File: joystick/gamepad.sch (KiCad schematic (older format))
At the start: 37 parts, among them IC1 ATTINY45-S, P2 CONN_01X04, SW1 SW_PUSH, SW2 SW_PUSH, SW3 SW_PUSH, SW4 SW_PUSH, SW5 SW_PUSH, SW6 SW_PUSH, U1 74LS165, U2 74164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

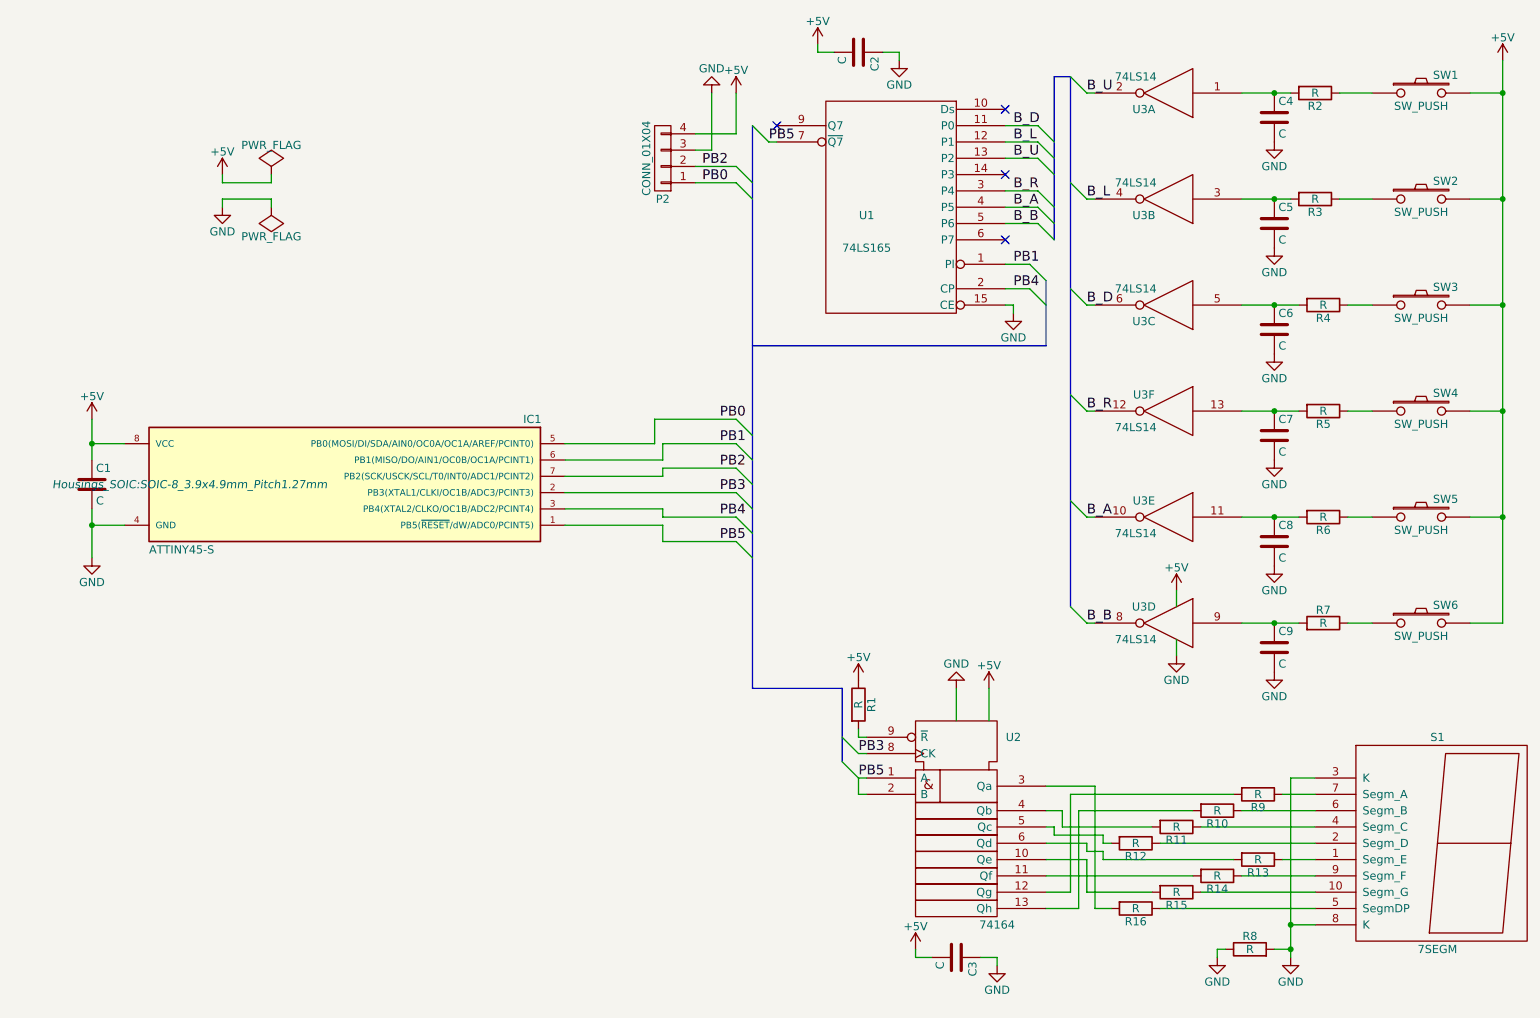
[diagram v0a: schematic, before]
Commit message: Updated joystick's circuit
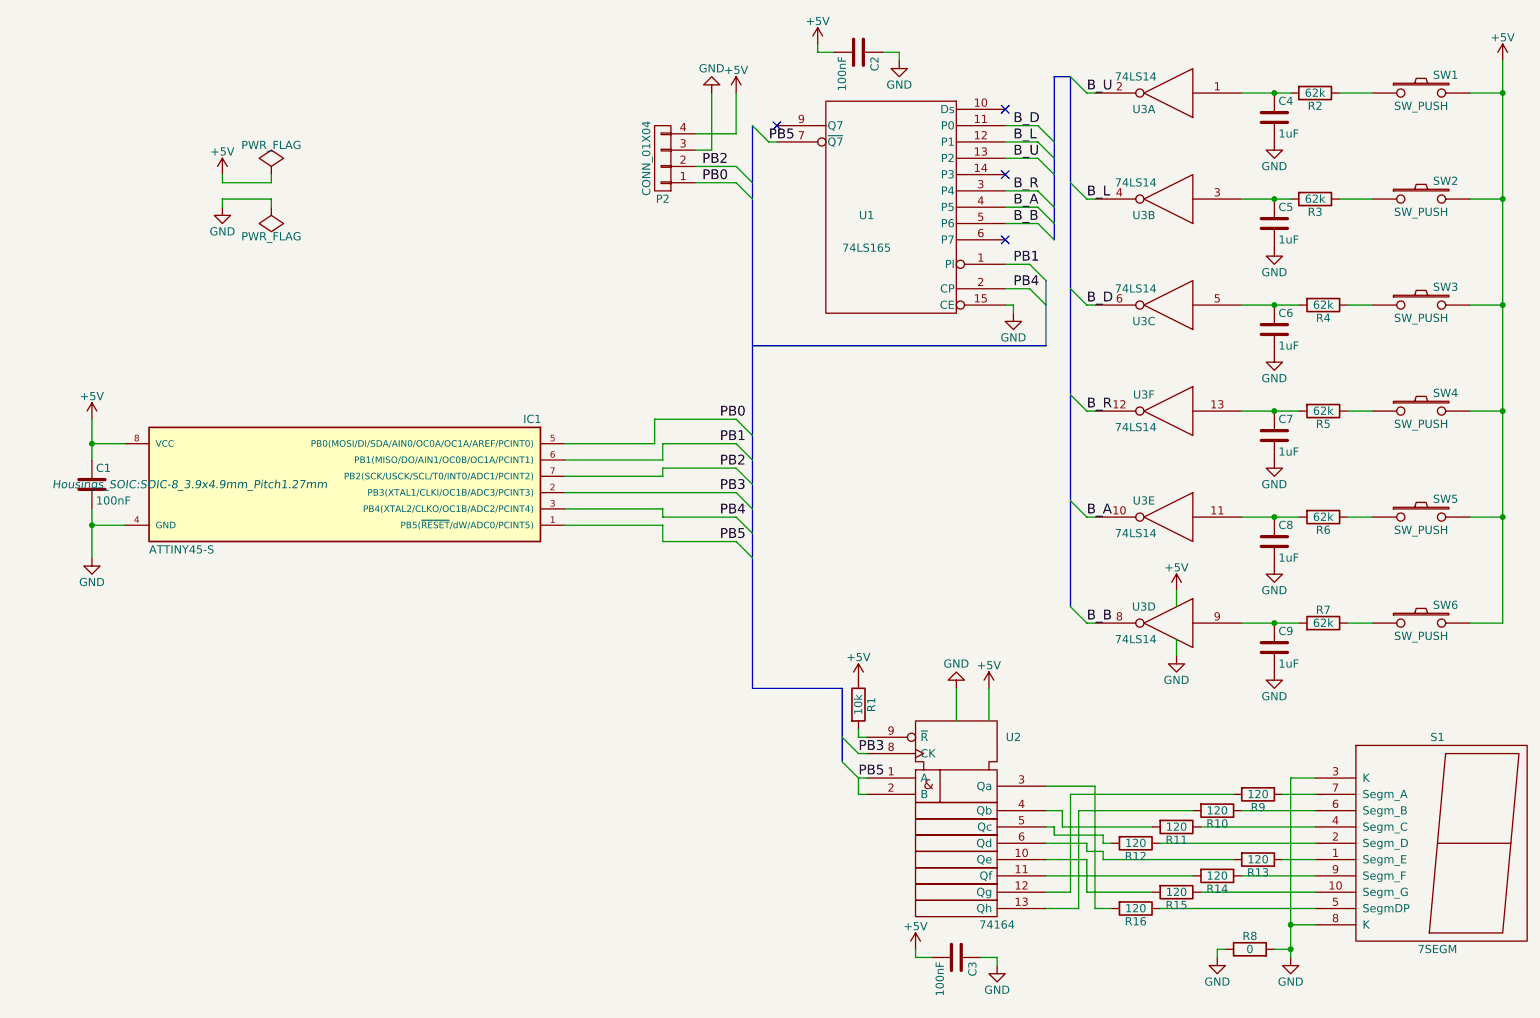
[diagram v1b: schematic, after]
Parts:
- C1, C2, C3: value C -> 100nF
- C4, C5, C6, C7, C8, C9: value C -> 1uF
- R1: value R -> 10k
- R10, R11, R12, R13, R14, R15, R16, R9: value R -> 120
- R2, R3, R4, R5, R6, R7: value R -> 62k
- R8: value R -> 0
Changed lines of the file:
@@
 P 8150 1000
 F 0 "R2" V 8230 1000 50  0000 C CNN
-F 1 "R" V 8150 1000 50  0000 C CNN
+F 1 "62k" V 8150 1000 50  0000 C CNN
 F 2 "Resistors_SMD:R_0805_HandSoldering" V 8080 1000 50  0001 C CNN
 F 3 "" H 8150 1000 50  0000 C CNN
@@
 P 7900 1150
 F 0 "C4" H 7925 1250 50  0000 L CNN
-F 1 "C" H 7925 1050 50  0000 L CNN
+F 1 "1uF" H 7925 1050 50  0000 L CNN
 F 2 "Capacitors_SMD:C_0805_HandSoldering" H 7938 1000 50  0001 C CNN
 F 3 "" H 7900 1150 50  0000 C CNN
@@
 P 8150 1650
 F 0 "R3" V 8230 1650 50  0000 C CNN
-F 1 "R" V 8150 1650 50  0000 C CNN
+F 1 "62k" V 8150 1650 50  0000 C CNN
 F 2 "Resistors_SMD:R_0805_HandSoldering" V 8080 1650 50  0001 C CNN
 F 3 "" H 8150 1650 50  0000 C CNN
@@
 P 7900 1800
 F 0 "C5" H 7925 1900 50  0000 L CNN
-F 1 "C" H 7925 1700 50  0000 L CNN
+F 1 "1uF" H 7925 1700 50  0000 L CNN
 F 2 "Capacitors_SMD:C_0805_HandSoldering" H 7938 1650 50  0001 C CNN
 F 3 "" H 7900 1800 50  0000 C CNN
@@
 P 7900 2450
 F 0 "C6" H 7925 2550 50  0000 L CNN
-F 1 "C" H 7925 2350 50  0000 L CNN
+F 1 "1uF" H 7925 2350 50  0000 L CNN
 F 2 "Capacitors_SMD:C_0805_HandSoldering" H 7938 2300 50  0001 C CNN
 F 3 "" H 7900 2450 50  0000 C CNN
@@
 P 8200 2300
 F 0 "R4" V 8280 2300 50  0000 C CNN
-F 1 "R" V 8200 2300 50  0000 C CNN
+F 1 "62k" V 8200 2300 50  0000 C CNN
 F 2 "Resistors_SMD:R_0805_HandSoldering" V 8130 2300 50  0001 C CNN
 F 3 "" H 8200 2300 50  0000 C CNN
@@
 P 7900 3100
 F 0 "C7" H 7925 3200 50  0000 L CNN
-F 1 "C" H 7925 3000 50  0000 L CNN
+F 1 "1uF" H 7925 3000 50  0000 L CNN
 F 2 "Capacitors_SMD:C_0805_HandSoldering" H 7938 2950 50  0001 C CNN
 F 3 "" H 7900 3100 50  0000 C CNN
@@
 P 8200 2950
 F 0 "R5" V 8280 2950 50  0000 C CNN
-F 1 "R" V 8200 2950 50  0000 C CNN
+F 1 "62k" V 8200 2950 50  0000 C CNN
 F 2 "Resistors_SMD:R_0805_HandSoldering" V 8130 2950 50  0001 C CNN
 F 3 "" H 8200 2950 50  0000 C CNN
@@
 P 7900 3750
 F 0 "C8" H 7925 3850 50  0000 L CNN
-F 1 "C" H 7925 3650 50  0000 L CNN
+F 1 "1uF" H 7925 3650 50  0000 L CNN
 F 2 "Capacitors_SMD:C_0805_HandSoldering" H 7938 3600 50  0001 C CNN
 F 3 "" H 7900 3750 50  0000 C CNN
@@
 P 8200 3600
 F 0 "R6" V 8280 3600 50  0000 C CNN
-F 1 "R" V 8200 3600 50  0000 C CNN
+F 1 "62k" V 8200 3600 50  0000 C CNN
 F 2 "Resistors_SMD:R_0805_HandSoldering" V 8130 3600 50  0001 C CNN
 F 3 "" H 8200 3600 50  0000 C CNN
@@
 P 7900 4400
 F 0 "C9" H 7925 4500 50  0000 L CNN
-F 1 "C" H 7925 4300 50  0000 L CNN
+F 1 "1uF" H 7925 4300 50  0000 L CNN
 F 2 "Capacitors_SMD:C_0805_HandSoldering" H 7938 4250 50  0001 C CNN
 F 3 "" H 7900 4400 50  0000 C CNN
@@
 P 8200 4250
 F 0 "R7" V 8280 4250 50  0000 C CNN
-F 1 "R" V 8200 4250 50  0000 C CNN
+F 1 "62k" V 8200 4250 50  0000 C CNN
 F 2 "Resistors_SMD:R_0805_HandSoldering" V 8130 4250 50  0001 C CNN
 F 3 "" H 8200 4250 50  0000 C CNN
@@
 P 650 3400
 F 0 "C1" H 675 3500 50  0000 L CNN
-F 1 "C" H 675 3300 50  0000 L CNN
+F 1 "100nF" H 675 3300 50  0000 L CNN
 F 2 "Capacitors_SMD:C_0805_HandSoldering" H 688 3250 50  0001 C CNN
 F 3 "" H 650 3400 50  0000 C CNN
@@
 P 5350 4750
 F 0 "R1" V 5430 4750 50  0000 C CNN
-F 1 "R" V 5350 4750 50  0000 C CNN
+F 1 "10k" V 5350 4750 50  0000 C CNN
 F 2 "Resistors_SMD:R_0805_HandSoldering" V 5280 4750 50  0001 C CNN
 F 3 "" H 5350 4750 50  0000 C CNN
@@
 P 5950 6300
 F 0 "C3" H 5975 6400 50  0000 L CNN
-F 1 "C" H 5975 6200 50  0000 L CNN
+F 1 "100nF" H 5975 6200 50  0000 L CNN
 F 2 "Capacitors_SMD:C_0805_HandSoldering" H 5988 6150 50  0001 C CNN
 F 3 "" H 5950 6300 50  0000 C CNN
@@
 P 5350 750
 F 0 "C2" H 5375 850 50  0000 L CNN
-F 1 "C" H 5375 650 50  0000 L CNN
+F 1 "100nF" H 5375 650 50  0000 L CNN
 F 2 "Capacitors_SMD:C_0805_HandSoldering" H 5388 600 50  0001 C CNN
 F 3 "" H 5350 750 50  0000 C CNN
@@
 P 7750 6250
 F 0 "R8" V 7830 6250 50  0000 C CNN
-F 1 "R" V 7750 6250 50  0000 C CNN
+F 1 "0" V 7750 6250 50  0000 C CNN
 F 2 "Resistors_SMD:R_0805_HandSoldering" V 7680 6250 50  0001 C CNN
 F 3 "" H 7750 6250 50  0000 C CNN
@@
 P 7800 5300
 F 0 "R9" V 7880 5300 50  0000 C CNN
-F 1 "R" V 7800 5300 50  0000 C CNN
+F 1 "120" V 7800 5300 50  0000 C CNN
 F 2 "Resistors_SMD:R_0805_HandSoldering" V 7730 5300 50  0001 C CNN
 F 3 "" H 7800 5300 50  0000 C CNN
@@
 P 7550 5400
 F 0 "R10" V 7630 5400 50  0000 C CNN
-F 1 "R" V 7550 5400 50  0000 C CNN
+F 1 "120" V 7550 5400 50  0000 C CNN
 F 2 "Resistors_SMD:R_0805_HandSoldering" V 7480 5400 50  0001 C CNN
 F 3 "" H 7550 5400 50  0000 C CNN
@@
 P 7300 5500
 F 0 "R11" V 7380 5500 50  0000 C CNN
-F 1 "R" V 7300 5500 50  0000 C CNN
+F 1 "120" V 7300 5500 50  0000 C CNN
 F 2 "Resistors_SMD:R_0805_HandSoldering" V 7230 5500 50  0001 C CNN
 F 3 "" H 7300 5500 50  0000 C CNN
@@
 P 7050 5600
 F 0 "R12" V 7130 5600 50  0000 C CNN
-F 1 "R" V 7050 5600 50  0000 C CNN
+F 1 "120" V 7050 5600 50  0000 C CNN
 F 2 "Resistors_SMD:R_0805_HandSoldering" V 6980 5600 50  0001 C CNN
 F 3 "" H 7050 5600 50  0000 C CNN
@@
 P 7800 5700
 F 0 "R13" V 7880 5700 50  0000 C CNN
-F 1 "R" V 7800 5700 50  0000 C CNN
+F 1 "120" V 7800 5700 50  0000 C CNN
 F 2 "Resistors_SMD:R_0805_HandSoldering" V 7730 5700 50  0001 C CNN
 F 3 "" H 7800 5700 50  0000 C CNN
@@
 P 7550 5800
 F 0 "R14" V 7630 5800 50  0000 C CNN
-F 1 "R" V 7550 5800 50  0000 C CNN
+F 1 "120" V 7550 5800 50  0000 C CNN
 F 2 "Resistors_SMD:R_0805_HandSoldering" V 7480 5800 50  0001 C CNN
 F 3 "" H 7550 5800 50  0000 C CNN
@@
 P 7300 5900
 F 0 "R15" V 7380 5900 50  0000 C CNN
-F 1 "R" V 7300 5900 50  0000 C CNN
+F 1 "120" V 7300 5900 50  0000 C CNN
 F 2 "Resistors_SMD:R_0805_HandSoldering" V 7230 5900 50  0001 C CNN
 F 3 "" H 7300 5900 50  0000 C CNN
@@
 P 7050 6000
 F 0 "R16" V 7130 6000 50  0000 C CNN
-F 1 "R" V 7050 6000 50  0000 C CNN
+F 1 "120" V 7050 6000 50  0000 C CNN
 F 2 "Resistors_SMD:R_0805_HandSoldering" V 6980 6000 50  0001 C CNN
 F 3 "" H 7050 6000 50  0000 C CNN
